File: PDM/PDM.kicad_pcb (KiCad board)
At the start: 4 copper layers, 120 x 95 mm, 229 parts, among them J1 HCCPHPE24BKA90F, J2 M6 VBAT, Q1 BSS84, Q2 BSP75N, U1 LM2937IMP-5.0, U10 BTS7002-1EPP, U11 BTS7002-1EPP, U12 BTS7002-1EPP, U13 BTS7002-1EPP, U14 BTS7002-1EPP, U15 BTS7002-1EPP, U16 BTS7002-1EPP, U17 BTS7002-1EPP, U2 LMR36520ADDAR, U3 74HC86-Q100, U4 74HC86-Q100, U5 LM2901AVQDR (-Q1), U6 LM2901AVQDR (-Q1), U7 LM2901AVQDR (-Q1), U8 LM2901AVQDR (-Q1), U9 LM2901AVQDR (-Q1)

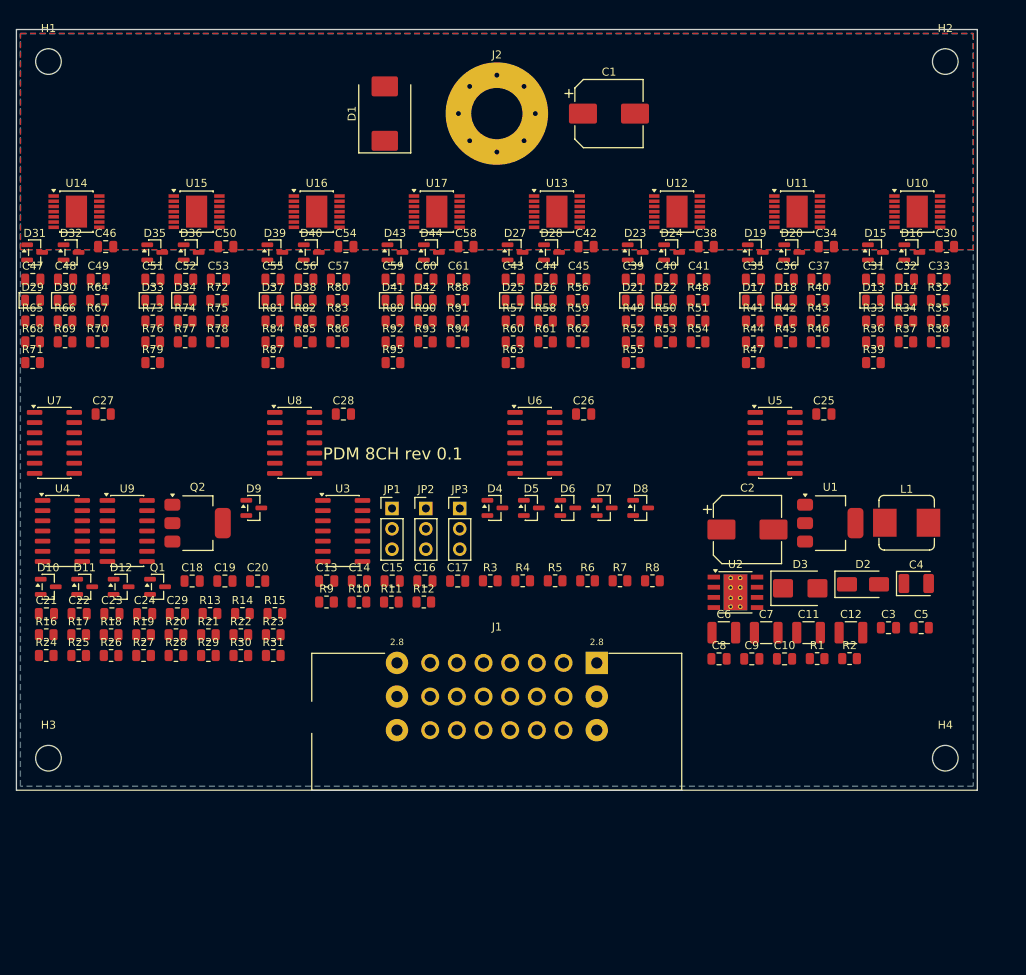
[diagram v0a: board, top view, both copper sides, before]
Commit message: PDM: autorouted 4-layer PCB (124x106 mm)
- New floorplan: 8x BTS7002 in a row right above the Aptiv connector,
  OUT pins facing down; logic / inputs / 5V supply / VBAT stud on top
- Output copper as per-channel zones on up to 4 layers to J1 pins
  (A1+A2 CH1 ... C8 CH6), 29-via arrays under each BTS tie the layers
- In2 = solid VBAT plane (stud -> BTS tabs, 8 thermal vias per EP),
  kept free of signals; In1 = GND plane (also carries some signals)
- Net classes Supply 0.6 mm / HighCurrent 1.5 mm, 0.15 mm neck-down rule
- Signals autorouted with Freerouting 2.4.1 (tools/dsn.py, ses.py)
- DRC: 0 errors, 0 schematic parity issues, 4 short signal links left
  to route by hand (REF_25, IS8, C32 and C36 branch to OUT1/OUT2)

Co-Authored-By: Claude Opus 5.5 <noreply@anthropic.com>
Claude-Session: https://claude.ai/code/session_011RdW2Ae3jMjzHoNbLtu1MC
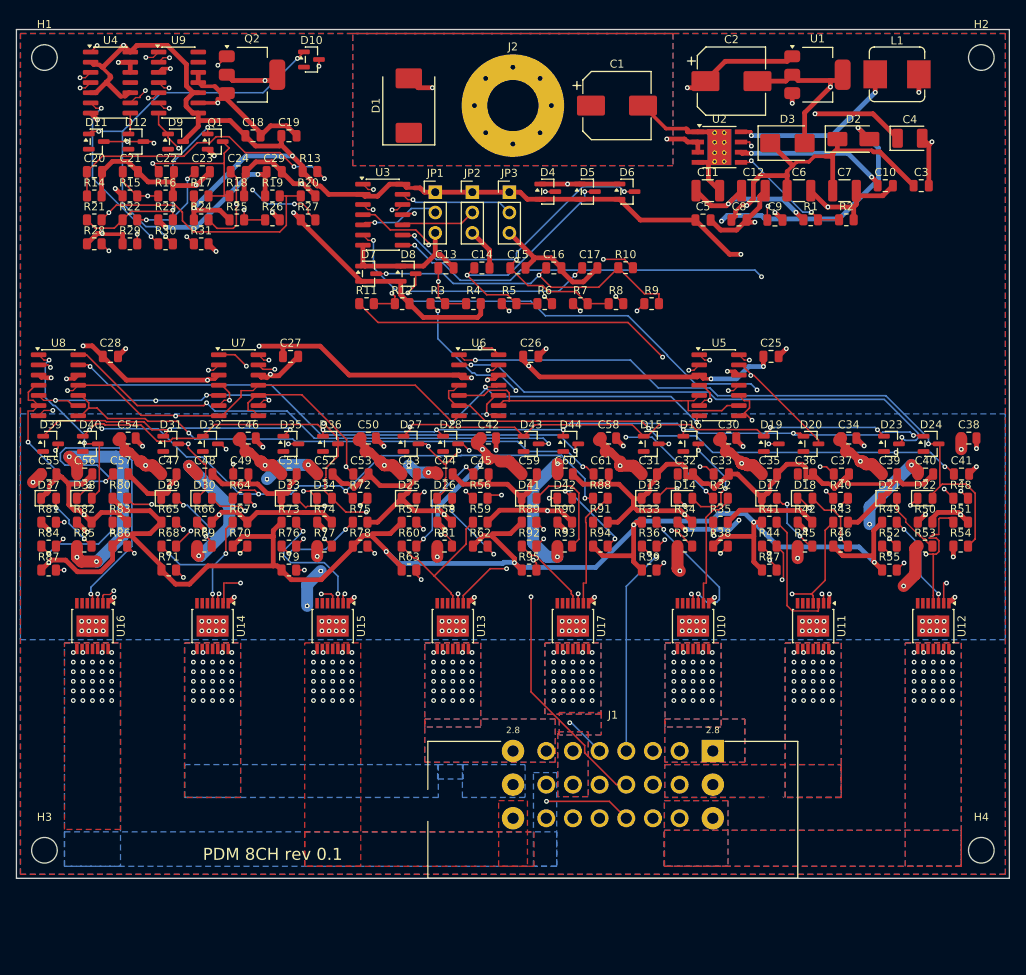
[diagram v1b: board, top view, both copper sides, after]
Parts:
- moved D10 73.6 mm to (136.8, 53.7)
- moved U12 60.8 mm to (214.5, 124.5), turned to -90 degrees
- moved C10 60.4 mm to (208.5, 69.5)
- moved U10 58.8 mm to (184.5, 124.5), turned to -90 degrees
- moved U16 58.8 mm to (109.5, 124.5), turned to -90 degrees
- moved R27 58.2 mm to (136.4, 73.8)
- moved R26 58.0 mm to (132.0, 73.8)
- moved R25 57.9 mm to (127.5, 73.8)
- moved C5 57.7 mm to (185.7, 73.8)
- moved R24 57.7 mm to (123.1, 73.8)
- moved R20 57.2 mm to (136.4, 70.8)
- moved R19 57.1 mm to (132.0, 70.8)
- moved R18 57.0 mm to (127.5, 70.8)
- moved R17 56.9 mm to (123.1, 70.8)
- moved R16 56.8 mm to (118.6, 70.8)
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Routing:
- net /+5V: track 0.00 -> 503.6 mm, vias 0 -> 17
- net /GND: track 0.00 -> 430.3 mm, vias 0 -> 28
- net /VKEY: track 0.00 -> 276.6 mm, vias 0 -> 15
- net /FLTB_ANY_N: track 0.00 -> 194.6 mm, vias 0 -> 9
- net /OVL_ANY_N: track 0.00 -> 171.4 mm, vias 0 -> 7
- net /REF_FLT: track 0.00 -> 157.5 mm, vias 0 -> 8
- net /+5V_DISP: track 0.00 -> 128.1 mm, vias 0 -> 3
- net /IN_MAIN_CMD: track 0.00 -> 126.4 mm, vias 0 -> 5
- net /LAMP: track 0.00 -> 123.0 mm, vias 0 -> 1
- net /VKEY_RAW: track 0.00 -> 102.4 mm, vias 0 -> 2
- net /IN_MAIN_F: track 0.00 -> 95.1 mm, vias 0 -> 4
- net /IN_MAIN_RAW: track 0.00 -> 91.8 mm, vias 0 -> 2
- net /FLT8_N: track 0.00 -> 85.8 mm, vias 0 -> 4
- net /IN3_CMD: track 0.00 -> 85.1 mm, vias 0 -> 3
- net /OVL8_N: track 0.00 -> 84.7 mm, vias 0 -> 4
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- added copper zone on F.Cu, net /GND
- added copper zone on B.Cu, net /OUT1
- added copper zone on F.Cu, net /OUT1
- added copper zone on In1.Cu, net /OUT1
- added copper zone on In2.Cu, net /OUT1
- added copper zone on B.Cu, net /OUT2
- added copper zone on F.Cu, net /OUT2
- added copper zone on In1.Cu, net /OUT2
- added copper zone on In2.Cu, net /OUT2
- added copper zone on B.Cu, net /OUT3
- added copper zone on F.Cu, net /OUT3
- added copper zone on In1.Cu, net /OUT3
- added copper zone on In2.Cu, net /OUT3
- added copper zone on B.Cu, net /OUT4
- added copper zone on F.Cu, net /OUT4
- added copper zone on In1.Cu, net /OUT4
- added copper zone on In2.Cu, net /OUT4
- added copper zone on B.Cu, net /OUT5
- added copper zone on F.Cu, net /OUT5
- added copper zone on In2.Cu, net /OUT5
- added copper zone on F.Cu, net /OUT6
- added copper zone on In1.Cu, net /OUT6
- added copper zone on B.Cu, net /OUT7
- added copper zone on F.Cu, net /OUT7
- added copper zone on In2.Cu, net /OUT7
- added copper zone on B.Cu, net /OUT8
- added copper zone on F.Cu, net /OUT8
- added copper zone on In1.Cu, net /OUT8
- added copper zone on In2.Cu, net /OUT8
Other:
- board size 120 x 95 mm -> 124 x 106 mm

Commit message: PDM PCB: updated to the revised schematic, re-routed
- 5V buck removed from the board, F1 PTC (+12V_DISP), VCOMP R96/D45/C62
  and R97 placed in the supply group; net classes updated
- In1 GND_TIE strip between OUT8 and OUT1 copper keeps J1 B3/C3 tied to
  the GND plane (router may not cut it)
- ~340 GND stitching vias (tools/stitch.py) tie F.Cu/B.Cu GND fill to In1
- tools/join.py closes leftover islands with DRC-checked short links
  (reconnected the IS6 sense resistor ground)
- DRC: 0 errors, 0 parity issues; 7 short signal links left to route by
  hand: FLT7_N, FLTB_ANY_N, IN4_F, IN_MAIN_CMD, C32/C44/C56 to OUT1/4/7
- docs/PDM_schema.pdf added

Co-Authored-By: Claude Opus 5.5 <noreply@anthropic.com>
Claude-Session: https://claude.ai/code/session_011RdW2Ae3jMjzHoNbLtu1MC
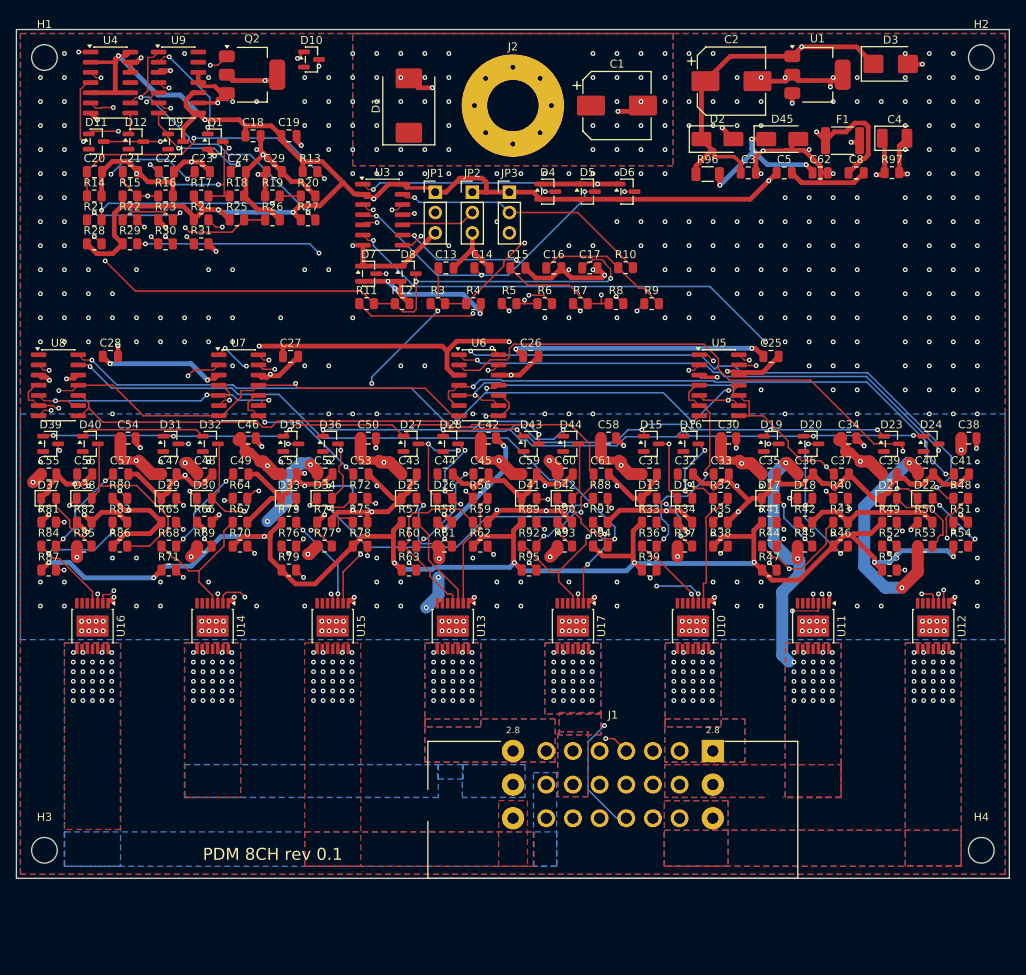
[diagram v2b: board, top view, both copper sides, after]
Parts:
- removed C10: 1u/16V, Capacitor_SMD:C_0805_2012Metric
- removed C11, C12: 22u/25V, Capacitor_SMD:C_1210_3225Metric
- removed C6, C7: 4u7/100V, Capacitor_SMD:C_1210_3225Metric
- removed C9: 100n/16V, Capacitor_SMD:C_0805_2012Metric
- removed L1: 10u Isat>=3.6A, Inductor_SMD:L_Bourns_SRP7028A_7.3x6.6mm
- removed R1: 100k 1%, Resistor_SMD:R_0805_2012Metric
- removed R2: 24k9 1%, Resistor_SMD:R_0805_2012Metric
- removed U2: LMR36520ADDAR, Package_SO:TI_SO-PowerPAD-8_ThermalVias
- added C62: 1u/50V, Capacitor_SMD:C_0805_2012Metric, F.Cu at (200.4, 67.9)
- added D45: 18V 1W SMAZ18, Diode_SMD:D_SMA, F.Cu at (195.6, 63.7)
- added F1: 0.5A PTC 1812L050/33, Fuse:Fuse_1812_4532Metric, F.Cu at (203.2, 63.9)
- added R96: 470R, Resistor_SMD:R_1206_3216Metric, F.Cu at (186.3, 68.1)
- added R97: 1k, Resistor_SMD:R_0805_2012Metric, F.Cu at (209.3, 67.9)
- C23: value 220n -> 330n
- R17: value 6k81 1% -> 68k1 1%
- R18: value 10k 1% -> 100k 1%
- R23: value 4k7 -> 22k
- moved C3 21.7 mm to (191.4, 67.9)
- moved D2 17.0 mm to (187.5, 63.7)
- moved D3 16.2 mm to (209.2, 54.3)
- moved C8 15.8 mm to (204.9, 67.9)
- moved C5 11.7 mm to (195.9, 67.9)
- moved C4 1.90 mm to (209.7, 63.6)
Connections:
- C25 pad 1: /VKEY -> /VCOMP
- C26 pad 1: /VKEY -> /VCOMP
- C27 pad 1: /VKEY -> /VCOMP
- C28 pad 1: /VKEY -> /VCOMP
- C29 pad 1: /VKEY -> /VCOMP
- J1 pad C6: /+5V_DISP -> /+12V_DISP
- Q1 pad 2: /VKEY -> /VCOMP
- R19 pad 1: /VKEY -> /VCOMP
- R23 pad 1: /VKEY -> /VCOMP
- U5 pad 3: /VKEY -> /VCOMP
- U6 pad 3: /VKEY -> /VCOMP
- U7 pad 3: /VKEY -> /VCOMP
- U8 pad 3: /VKEY -> /VCOMP
- U9 pad 3: /VKEY -> /VCOMP
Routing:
- net /VCOMP: track 0.00 -> 219.2 mm, vias 0 -> 15
- net /VKEY: track 276.6 -> 69.1 mm, vias 15 -> 2
- net /+5V_DISP: track 128.1 -> 0.00 mm, vias 3 -> 0
- net /+12V_DISP: track 0.00 -> 110.3 mm, vias 0 -> 1
- net /REF_25: track 79.0 -> 119.1 mm, vias 2 -> 4
- net /GND: track 430.3 -> 391.9 mm, vias 28 -> 373
- net /IS7: track 56.3 -> 20.5 mm, vias 3 -> 2
- net /SW5: track 33.8 -> 0.00 mm, vias 3 -> 0
- net /OUT4: track 42.9 -> 14.8 mm
- net /OUT7: track 42.0 -> 15.8 mm, vias 32 -> 30
- net /IN_MAIN_CMD: track 126.4 -> 103.0 mm, vias 5 -> 4
- net /IN4_F: track 51.6 -> 28.2 mm, vias 3 -> 2
- net /FLT7_N: track 47.0 -> 25.0 mm, vias 3 -> 0
- net /IN1_RAW: track 72.8 -> 94.3 mm, vias 3 -> 2
- net /VKEY_RAW: track 102.4 -> 83.4 mm, vias 2 -> 1
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
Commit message: PDM PCB: fully routed, 124x116 mm
- Board 10 mm taller, more spacing between parts
- Per channel the OUT EMC cap, LED resistor and green LED sit on the edge
  of the output copper right below the BTS (connect through the copper,
  no long branch traces)
- Freerouting run without the optimizer stage (it hung), GND stitching
  over the whole board outside the output copper
- DRC: 0 errors, 0 unconnected items, 0 schematic parity issues
  (only silkscreen warnings left)

Co-Authored-By: Claude Opus 5.5 <noreply@anthropic.com>
Claude-Session: https://claude.ai/code/session_011RdW2Ae3jMjzHoNbLtu1MC
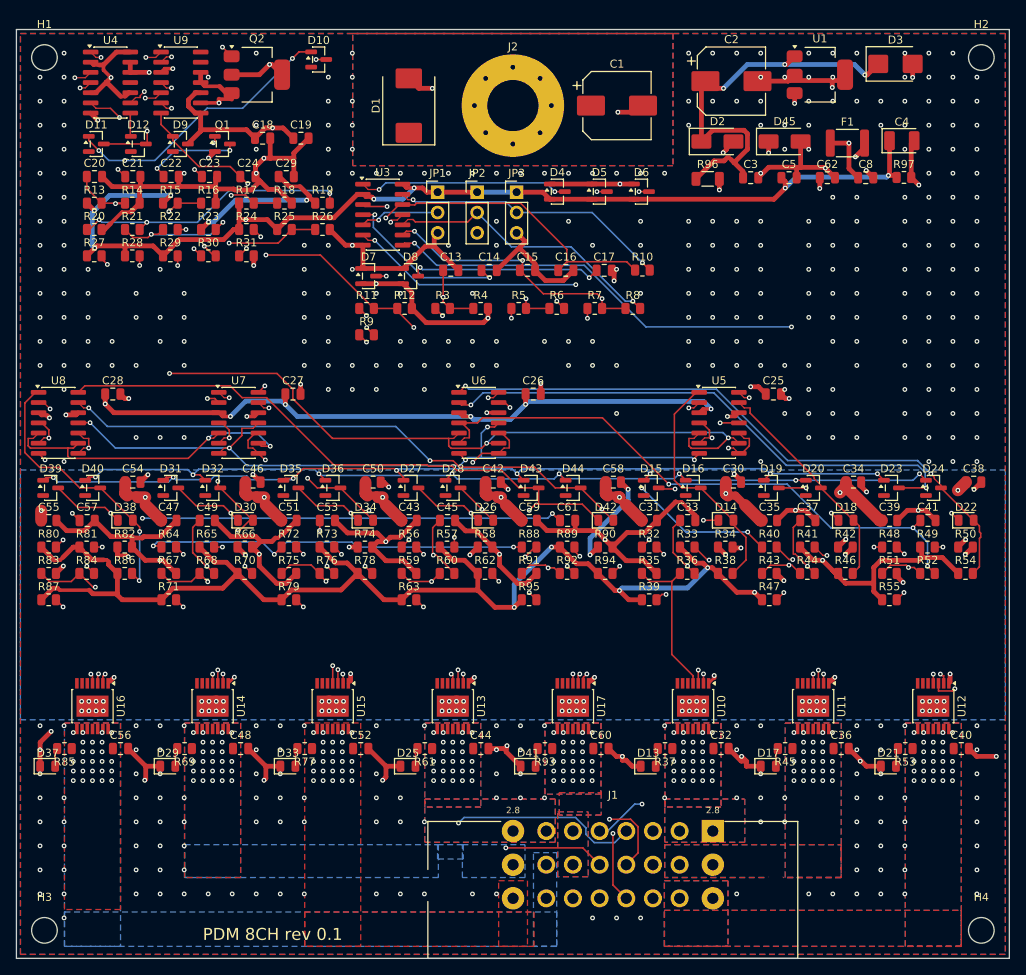
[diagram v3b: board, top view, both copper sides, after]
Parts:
- moved R9 35.8 mm to (143.7, 88.1)
- moved C32 34.6 mm to (188.0, 139.8)
- moved C36 34.6 mm to (203.0, 139.8)
- moved C40 34.6 mm to (218.0, 139.8)
- moved C44 34.6 mm to (158.0, 139.8)
- moved C48 34.6 mm to (128.0, 139.8)
- moved C52 34.6 mm to (143.0, 139.8)
- moved C56 34.6 mm to (113.0, 139.8)
- moved C60 34.6 mm to (173.0, 139.8)
- moved D13 33.5 mm to (178.9, 142.0)
- moved D17 33.5 mm to (193.9, 142.0)
- moved D21 33.5 mm to (208.9, 142.0)
- moved D25 33.5 mm to (148.9, 142.0)
- moved D29 33.5 mm to (118.9, 142.0)
- moved D33 33.5 mm to (133.9, 142.0)
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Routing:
- net /OUT3: track 38.7 -> 0.00 mm, vias 31 -> 25
- net /OUT6: track 37.3 -> 0.00 mm, vias 32 -> 25
- net /OUT2: track 32.3 -> 0.00 mm, vias 31 -> 25
- net /OUT5: track 29.9 -> 0.00 mm, vias 31 -> 25
- net /OUT8: track 28.5 -> 0.00 mm, vias 31 -> 25
- net /IN4_F: track 28.2 -> 55.1 mm, vias 2 -> 3
- net /+12V_DISP: track 110.3 -> 136.6 mm
- net /OVL_ANY_N: track 166.1 -> 191.1 mm, vias 9 -> 10
- net /OVL2_N: track 33.8 -> 58.1 mm
- net /GND: track 391.9 -> 367.9 mm, vias 373 -> 453
- net /LAMP: track 121.0 -> 144.3 mm
- net /IN4_RAW: track 63.4 -> 84.5 mm, vias 1 -> 2
- net /OVL7_N: track 32.2 -> 50.4 mm, vias 4 -> 3
- net /OUT1: track 17.5 -> 0.00 mm, vias 30 -> 25
- net /FLT5_N: track 44.1 -> 27.7 mm
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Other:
- board size 124 x 106 mm -> 124 x 116 mm
